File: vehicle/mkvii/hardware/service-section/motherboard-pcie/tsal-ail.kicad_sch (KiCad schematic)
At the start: 4 parts, among them J201 pcie_x1, J202 TSAL/AIL HV

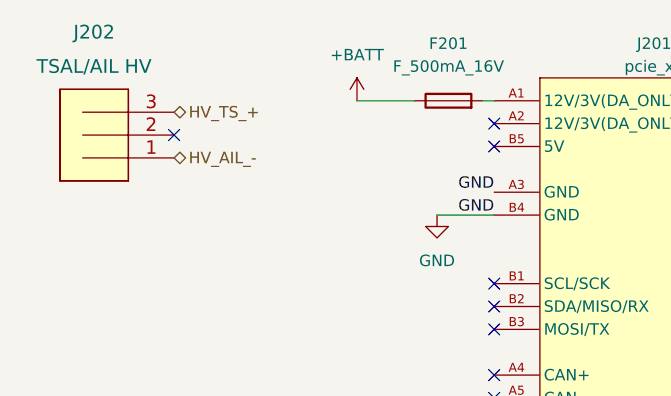
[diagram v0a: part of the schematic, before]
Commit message: first entirely complete draft w updated shdn and imd output
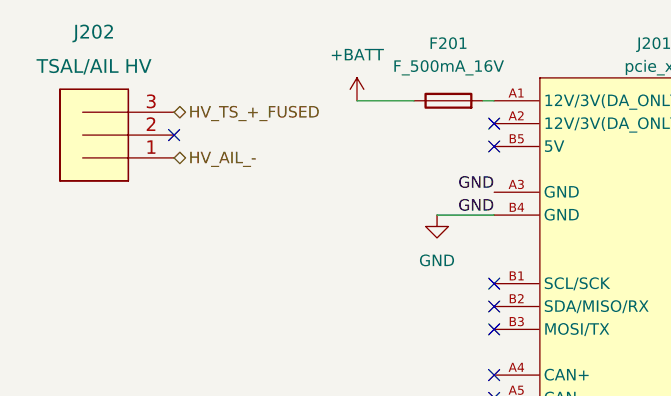
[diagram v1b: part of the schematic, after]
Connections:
- net HV_TS_+ renamed HV_TS_+_FUSED
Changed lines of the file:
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@@
     (effects (font (size 1.27 1.27)) (justify left))
   )
-  (hierarchical_label "HV_TS_+" (shape bidirectional) (at 93.98 78.74 0) (fields_autoplaced)
+  (hierarchical_label "HV_TS_+_FUSED" (shape bidirectional) (at 93.98 78.74 0) (fields_autoplaced)
     (effects (font (size 1.27 1.27)) (justify left))
   )

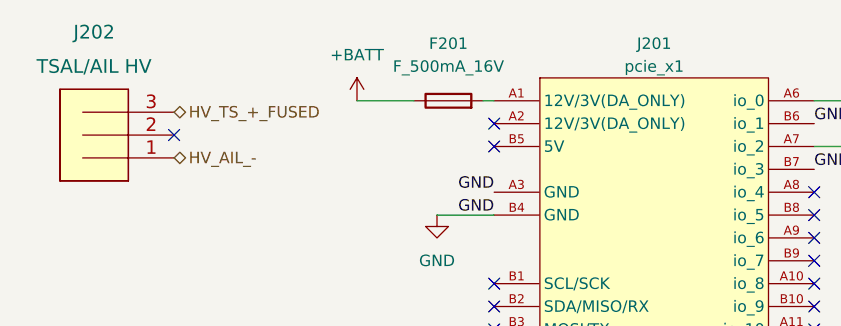
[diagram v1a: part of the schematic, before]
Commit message: renamed hierarchical sheets to reflect shdn changes, corrected ERC errors and annotated
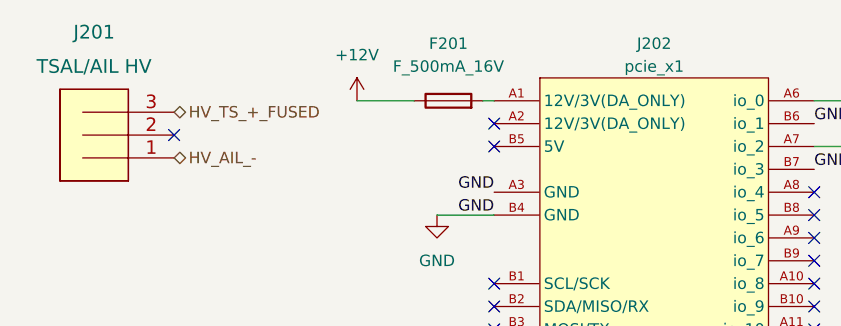
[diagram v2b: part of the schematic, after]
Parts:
- renumbered J202 to J201, J201 to J202
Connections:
- net +BATT renamed +12V
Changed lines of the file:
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@@
     (effects (font (size 1.27 1.27)) (justify left))
+  )
+  (symbol (lib_id "power:+12V") (at 114.3 77.47 0) (unit 1)
+    (in_bom yes) (on_board yes) (dnp no) (fields_autoplaced)
+    (property "Reference" "#PWR0201" (at 114.3 81.28 0)
+      (effects (font (size 1.27 1.27)) hide)
+    )
+    (property "Value" "+12V" (at 114.3 72.39 0)
+      (effects (font (size 1.27 1.27)))
+    )
+    (property "Footprint" "" (at 114.3 77.47 0)
+      (effects (font (size 1.27 1.27)) hide)
+    )
+    (property "Datasheet" "" (at 114.3 77.47 0)
+      (effects (font (size 1.27 1.27)) hide)
+    )
+    (pin "1")
+    (instances
+      (project "motherboard-pcie"
+        (path "/8f26d479-2c33-489f-a4df-6bb31c904ceb/a79abbba-3db4-4d37-af6c-322d54dae847"
+          (reference "#PWR0201") (unit 1)
+        )
+      )
+    )
   )
   (symbol (lib_id "OEM:F_500mA_16V") (at 124.46 77.47 90) (unit 1)
@@
   (symbol (lib_id "OEM:pcie_x1") (at 147.32 101.6 0) (unit 1)
     (in_bom yes) (on_board yes) (dnp no) (fields_autoplaced)
-    (property "Reference" "J201" (at 147.32 71.12 0) (do_not_autoplace)
+    (property "Reference" "J202" (at 147.32 71.12 0) (do_not_autoplace)
       (effects (font (size 1.27 1.27)))
     )
@@
       (project "motherboard-pcie"
         (path "/8f26d479-2c33-489f-a4df-6bb31c904ceb/a79abbba-3db4-4d37-af6c-322d54dae847"
-          (reference "J201") (unit 1)
+          (reference "J202") (unit 1)
         )
       )
@@
   (symbol (lib_id "oem:MicroFit_VT_3x1") (at 93.98 83.82 180) (unit 1)
     (in_bom yes) (on_board yes) (dnp no) (fields_autoplaced)
-    (property "Reference" "J202" (at 85.09 69.85 0)
+    (property "Reference" "J201" (at 85.09 69.85 0)
       (effects (font (size 1.524 1.524)))
     )
@@
       (project "motherboard-pcie"
         (path "/8f26d479-2c33-489f-a4df-6bb31c904ceb/a79abbba-3db4-4d37-af6c-322d54dae847"
-          (reference "J202") (unit 1)
-        )
-      )
-    )
-  )
-  (symbol (lib_id "power:+BATT") (at 114.3 77.47 0) (unit 1)
-    (in_bom yes) (on_board yes) (dnp no) (fields_autoplaced)
-    (property "Reference" "#PWR0201" (at 114.3 81.28 0)
-      (effects (font (size 1.27 1.27)) hide)
-    )
-    (property "Value" "+BATT" (at 114.3 72.39 0)
-      (effects (font (size 1.27 1.27)))
-    )
-    (property "Footprint" "" (at 114.3 77.47 0)
-      (effects (font (size 1.27 1.27)) hide)
-    )
-    (property "Datasheet" "" (at 114.3 77.47 0)
-      (effects (font (size 1.27 1.27)) hide)
-    )
-    (pin "1")
-    (instances
-      (project "motherboard-pcie"
-        (path "/8f26d479-2c33-489f-a4df-6bb31c904ceb/a79abbba-3db4-4d37-af6c-322d54dae847"
-          (reference "#PWR0201") (unit 1)
-        )
-      )
+          (reference "J201") (unit 1)
+        )
+      )
